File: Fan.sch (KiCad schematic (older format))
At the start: 0 parts

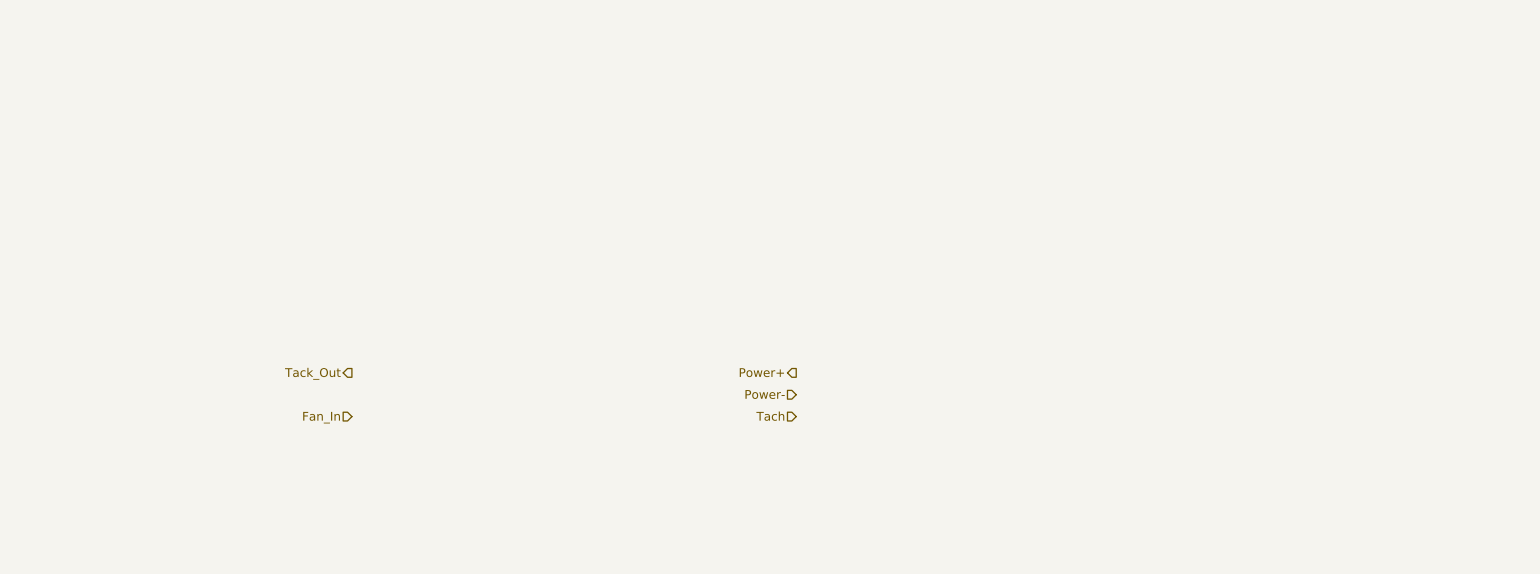
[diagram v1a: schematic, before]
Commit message: 3.4 Understanding The Current/Fan Driver Module Added circuit to the Current/Fan Driver module
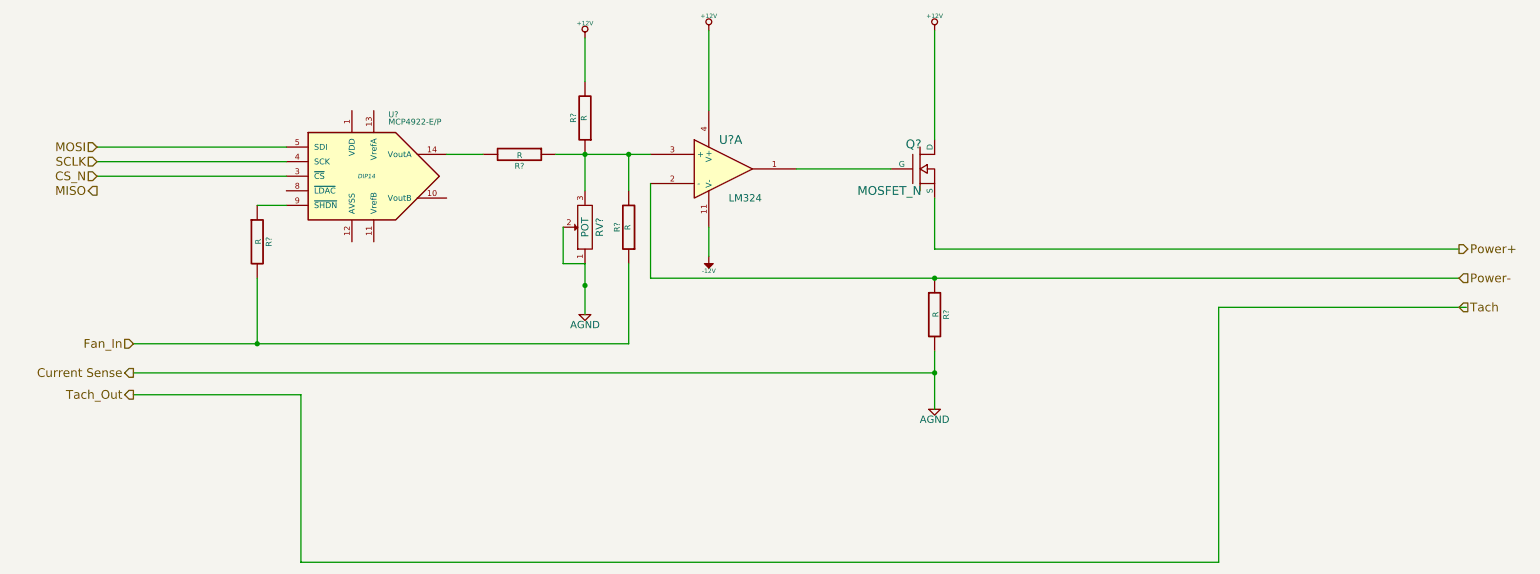
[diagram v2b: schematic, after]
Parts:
- added Q?: MOSFET_N, symbol MOSFET_N
- added R? (x5): R, symbol R
- added RV?: POT, symbol POT
- added U?: LM324, symbol LM324
- added U?: MCP4922-E/P, DIP14, symbol MCP4922-E/P
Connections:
- net Fan_In: now also R?.1, R?.2
- net Power+: now also Q?.S
- net Power-: now also R?.1, U?.2 (-)
- new net: Q?.G, U?.1
- new net: R?.1, R?.1, R?.2, RV?.3, U?.3 (+)
- new net: R?.2, U?.14 (VoutA)
- new net: R?.1, U?.9 (~SHDN~)
- new net +12V: Q?.D, R?.2, U?.4 (V+)
- new net -12V: U?.11 (V-)
- new net AGND: R?.2, RV?.1, RV?.2
- new net CS_N: U?.3 (~CS~)
- new net MOSI: U?.5 (SDI)
- new net SCLK: U?.4 (SCK)
